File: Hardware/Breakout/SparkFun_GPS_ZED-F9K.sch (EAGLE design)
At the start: 65 parts, among them J1 QWIIC_RIGHT_ANGLE, J4 U.FL, J6 QWIIC_RIGHT_ANGLE, U2 3.3V, U3 UBLOX_ZED_F9R

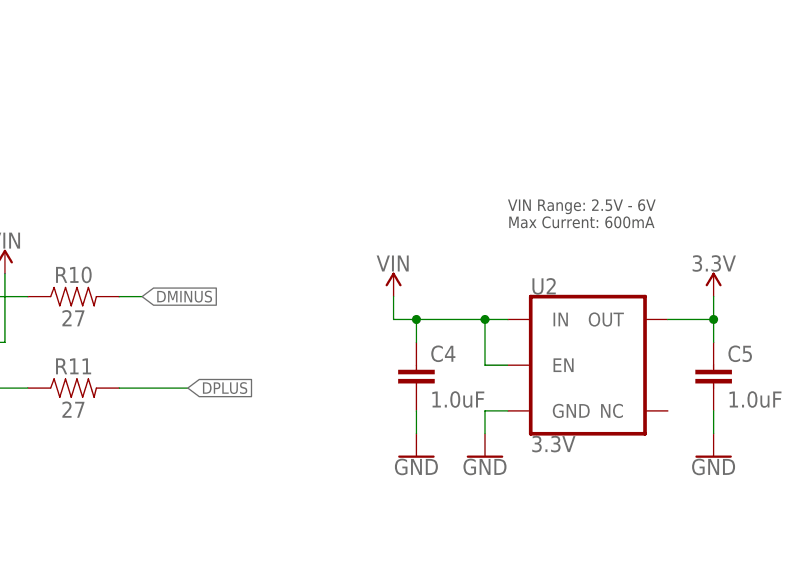
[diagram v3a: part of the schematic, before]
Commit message: Touches up some vias and traces
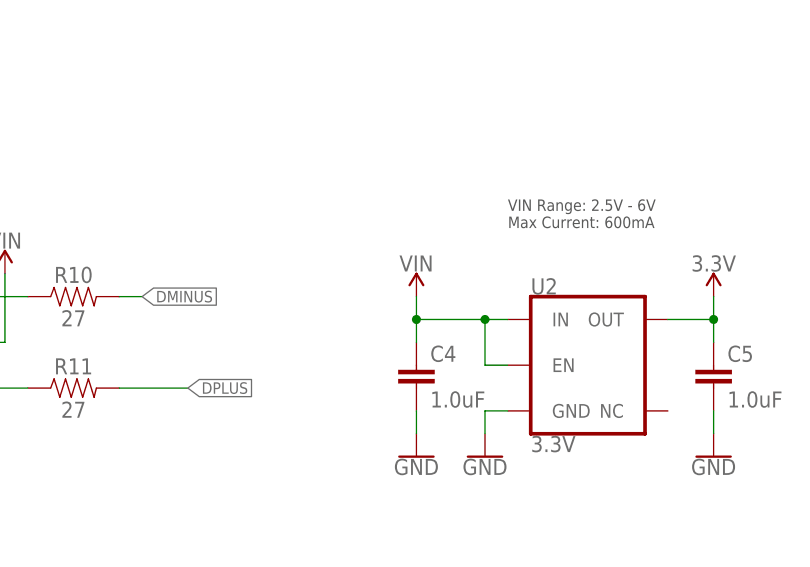
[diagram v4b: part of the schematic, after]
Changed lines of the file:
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@@
 <attribute name="VALUE" x="276.86" y="84.074" size="1.778" layer="96" align="bottom-center"/>
 </instance>
-<instance part="SUPPLY10" gate="G$1" x="276.86" y="228.6" smashed="yes">
-<attribute name="VALUE" x="276.86" y="231.394" size="1.778" layer="96" align="bottom-center"/>
+<instance part="SUPPLY10" gate="G$1" x="279.4" y="228.6" smashed="yes">
+<attribute name="VALUE" x="279.4" y="231.394" size="1.778" layer="96" align="bottom-center"/>
 </instance>
 <instance part="R5" gate="G$1" x="124.46" y="68.58" smashed="yes">
@@
 <wire x1="289.56" y1="226.06" x2="287.02" y2="226.06" width="0.1524" layer="91"/>
 <wire x1="287.02" y1="226.06" x2="279.4" y2="226.06" width="0.1524" layer="91"/>
-<wire x1="279.4" y1="226.06" x2="276.86" y2="226.06" width="0.1524" layer="91"/>
-<wire x1="276.86" y1="226.06" x2="276.86" y2="228.6" width="0.1524" layer="91"/>
+<wire x1="279.4" y1="226.06" x2="279.4" y2="228.6" width="0.1524" layer="91"/>
 <pinref part="U2" gate="G$1" pin="EN"/>
 <wire x1="289.56" y1="220.98" x2="287.02" y2="220.98" width="0.1524" layer="91"/>

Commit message: Gerbers for both boards
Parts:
- removed C5: 1.0uF, SparkFun-Capacitors:1.0UF-0603-16V-10%-X7R
- removed H3: STAND-OFFTIGHT, SparkFun-Hardware:STAND-OFFTIGHT
- removed J8: (no value), SparkFun-Connectors:CONN_09NO_SILK
- removed PPS, PWR: JUMPER-SMT_2_NC_TRACE_SILK, SparkFun-Jumpers:JUMPER-SMT_2_NC_TRACE_SILK
- added $1_36_$_2020-02-13_17-32-45: STAND-OFFTIGHT, SparkFun-Hardware:STAND-OFFTIGHT
- added C3: 1.0uF, SparkFun-Capacitors:1.0UF-0603-16V-10%-X7R
- added J7: (no value), SparkFun-Connectors:CONN_06NO_SILK_NO_POP
- added JP5: JUMPER-SMT_2_NO_SILK, SparkFun-Jumpers:JUMPER-SMT_2_NO_SILK
- added JP6: JUMPER-SMT_3_2-NC_TRACE_SILK, SparkFun-Jumpers:JUMPER-SMT_3_2-NC_TRACE_SILK
- C1: value 47pF -> 1.0uF; device SparkFun-Capacitors:47PF-0603-50V-5% -> SparkFun-Capacitors:1.0UF-0402-16V-10%
- C2: value 1.0uF -> 47pF; device SparkFun-Capacitors:1.0UF-0402-16V-10% -> SparkFun-Capacitors:47PF-0603-50V-5%
- D1: value 0.5A/40V/420mV -> RED; device SparkFun-DiscreteSemi:DIODE-SCHOTTKY-PMEG4005EJ -> SparkFun-LED:LED-RED0603
- D2: value RED -> BLUE; device SparkFun-LED:LED-RED0603 -> SparkFun-LED:LED-BLUE0603
- D4: value PRTR5V0U2F -> BLUE; device SparkFun-IC-Power:PRTR5V0U2F -> SparkFun-LED:LED-BLUE0603
- D5: value BLUE -> PRTR5V0U2F; device SparkFun-LED:LED-BLUE0603 -> SparkFun-IC-Power:PRTR5V0U2F
- D6: value BLUE -> 0.5A/40V/420mV; device SparkFun-LED:LED-BLUE0603 -> SparkFun-DiscreteSemi:DIODE-SCHOTTKY-PMEG4005EJ
- J1: value QWIIC_RIGHT_ANGLE -> U.FL; device SparkFun-Connectors:QWIIC_CONNECTORJS-1MM -> SparkFun-Connectors:U.FL2PIN
- J3: value (none) -> QWIIC_RIGHT_ANGLE; device SparkFun-Connectors:CONN_09NO_SILK -> SparkFun-Connectors:QWIIC_CONNECTORJS-1MM
- J4: value U.FL -> QWIIC_RIGHT_ANGLE; device SparkFun-Connectors:U.FL2PIN -> SparkFun-Connectors:QWIIC_CONNECTORJS-1MM
- J5: device SparkFun-Connectors:CONN_06NO_SILK_NO_POP -> SparkFun-Connectors:CONN_09NO_SILK
- J6: value QWIIC_RIGHT_ANGLE -> (none); device SparkFun-Connectors:QWIIC_CONNECTORJS-1MM -> SparkFun-Connectors:CONN_09NO_SILK
- JP1: value JUMPER-SMT_2_NO_SILK -> JUMPER-SMT_2_NC_TRACE_SILK; device SparkFun-Jumpers:JUMPER-SMT_2_NO_SILK -> SparkFun-Jumpers:JUMPER-SMT_2_NC_TRACE_SILK
- JP2: value JUMPER-SMT_3_2-NC_TRACE_SILK -> JUMPER-SMT_2_NC_TRACE_SILK; device SparkFun-Jumpers:JUMPER-SMT_3_2-NC_TRACE_SILK -> SparkFun-Jumpers:JUMPER-SMT_2_NC_TRACE_SILK
- LOGO1: value SFE_LOGO_NAME_FLAME.2_INCH -> OSHW-LOGOM; device SparkFun-Aesthetics:SFE_LOGO_NAME_FLAME.2_INCH -> SparkFun-Aesthetics:OSHW-LOGOM
- LOGO3: value OSHW-LOGOM -> SFE_LOGO_NAME_FLAME.2_INCH; device SparkFun-Aesthetics:OSHW-LOGOM -> SparkFun-Aesthetics:SFE_LOGO_NAME_FLAME.2_INCH
- R1: value 3.3k -> 100K; device SparkFun-Resistors:3.3KOHM-0603-1/10W-1% -> SparkFun-Resistors:100KOHM-0402-1/16W-1%
- R10, R11: value 27 -> 33; device SparkFun-Resistors:27OHM-0603-1/10W-1% -> SparkFun-Resistors:33OHM-0402-1/10W-1%
- R13, R14, R2: value 1KOHM-0402-1/16W-1% -> 33; device SparkFun-Resistors:1KOHM-0402-1/16W-1% -> SparkFun-Resistors:33OHM-0402-1/10W-1%
- R17: value 33 -> 10; device SparkFun-Resistors:33OHM-0402-1/10W-1% -> SparkFun-Resistors:10OHM-0603-1/10W-1%
- R18, R20: value 33 -> 5.1k; device SparkFun-Resistors:33OHM-0402-1/10W-1% -> SparkFun-Resistors:5.1KOHM-0402-1/16W-1%
- R19, R25: value 33 -> 2.2K; device SparkFun-Resistors:33OHM-0402-1/10W-1% -> SparkFun-Resistors:2.2KOHM-0402-1/16W-1%
- R21, R22, R23, R24: value 33 -> 1KOHM-0402-1/16W-1%; device SparkFun-Resistors:33OHM-0402-1/10W-1% -> SparkFun-Resistors:1KOHM-0402-1/16W-1%
- R26, R27: value 33 -> 27; device SparkFun-Resistors:33OHM-0402-1/10W-1% -> SparkFun-Resistors:27OHM-0603-1/10W-1%
- R28: value 1KOHM-0402-1/16W-1% -> 3.3k; device SparkFun-Resistors:1KOHM-0402-1/16W-1% -> SparkFun-Resistors:3.3KOHM-0603-1/10W-1%
- R3, R4: value 2.2K -> 33; device SparkFun-Resistors:2.2KOHM-0402-1/16W-1% -> SparkFun-Resistors:33OHM-0402-1/10W-1%
- R5: value 10 -> 33; device SparkFun-Resistors:10OHM-0603-1/10W-1% -> SparkFun-Resistors:33OHM-0402-1/10W-1%
- R6: value 100K -> 33; device SparkFun-Resistors:100KOHM-0402-1/16W-1% -> SparkFun-Resistors:33OHM-0402-1/10W-1%
- R8, R9: value 5.1k -> 33; device SparkFun-Resistors:5.1KOHM-0402-1/16W-1% -> SparkFun-Resistors:33OHM-0402-1/10W-1%
- renumbered B1 to BT1, FRAME2 to FRAME1, GEO to JP4, RTK to JP3, U3 to U1
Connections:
- net !RESET: now also J6.4, R4.2; no longer J8.4, R7.2
- net !SAFEBOOT: now also J6.3, R16.2; no longer J8.3, R25.2
- net 3.3V: now also C1.1, C4.1, D6.A, J3.2, J4.2, J5.3, J6.8, JP6.2, R1.2; no longer C2.1, C5.1, D2.A, J1.2, J3.3, J6.2, J8.8, JP2.2, R6.2
- net DIR: now also J5.8, R3.1; no longer J3.8, R27.1
- net DMINUS: now also R26.2; no longer R10.2
- net DPLUS: now also R27.2; no longer R11.2
- net D_SEL: now also JP5.1; no longer JP1.1
- net GEOF_STAT: now also D4.A, R13.2; no longer D3.A, R22.2
- net GND: now also C3.2, D5.2, J1.GND, J4.1, J6.9, J7.1, JP1.1, JP2.1, JP5.2, R1.1, R18.1, R20.1; no longer C5.2, D4.2, J1.1, J4.GND, J6.1, J8.9, JP1.2, PPS.1, PWR.1, R6.1, R8.1, R9.1
- net INT: now also J6.2, R5.2; no longer J8.2, R12.2
- net N$1: now also JP6.1, R25.2; no longer JP2.1, R3.2
- net N$10: now also D5.4, R27.1; no longer D4.4, R11.1
- net N$11: now also R4.1; no longer R7.1
- net N$12: now also R5.1; no longer R12.1
- net N$14: now also R18.2; no longer R8.2
- net N$15: now also R20.2; no longer R9.2
- net N$16: now also R6.1; no longer R15.1
- net N$17: now also R7.1; no longer R16.1
- net N$18: now also R8.1; no longer R17.1
- net N$19: now also R9.1; no longer R18.1
- net N$2: now also D6.C, R28.2; no longer D1.C, R1.2
- net N$20: now also R10.1; no longer R19.1
- net N$21: now also R11.1; no longer R20.1
- net N$22: now also R23.1; no longer R14.1
- net N$23: now also JP2.2, R22.1; no longer PPS.2, R13.1
- net N$24: now also D2.C, R22.2; no longer D5.C, R13.2
- net N$25: now also D3.C, R23.2; no longer D6.C, R14.2
- net N$26: now also R12.1; no longer R21.1
- net N$27: now also R13.1; no longer R22.1
- net N$28: now also R14.1; no longer R23.1
- net N$29: now also R15.1; no longer R24.1
- net N$3: now also JP6.3, R19.2; no longer JP2.3, R4.2
- net N$30: now also R16.1; no longer R25.1
- net N$31: now also R2.2; no longer R26.2
- net N$32: now also R3.2; no longer R27.2
- net N$33: now also R24.1; no longer R28.1
- net N$34: now also D4.C, R24.2; no longer D3.C, R28.2
- net N$4: now also D1.C, R21.2; no longer D2.C, R2.2
- net N$5: now also C2.1, R17.1; no longer C1.1, R5.1
- net N$6: now also D5.3; no longer D4.3
- net N$7: now also D5.1; no longer D4.1
- net N$8: now also JP1.2, R21.1; no longer PWR.2, R2.1
- net N$9: now also D5.6, R26.1; no longer D4.6, R10.1
- net PPS: now also D2.A, J6.1, R15.2; no longer D5.A, J8.1, R24.2
- net RF_IN: now also J1.SIGNAL; no longer J4.SIGNAL
- net RTK_STAT: now also D3.A, R14.2; no longer D6.A, R23.2
- net RXI/MOSI: now also J5.5, R10.2; no longer J3.5, R19.2
- net RXI2: now also J7.4, R12.2; no longer J5.4, R21.2
- net SCL/CLK: now also J3.4, J4.4, J5.7, J6.6, R19.1, R7.2; no longer J1.4, J3.7, J6.4, J8.6, R16.2, R4.1
- net SDA/!CS: now also J3.3, J4.3, J5.4, J6.7, R25.1, R6.2; no longer J1.3, J3.4, J6.3, J8.7, R15.2, R3.1
- net TXO/MISO: now also J5.6, R9.2; no longer J3.6, R18.2
- net TXO2: now also J7.5, R11.2; no longer J5.5, R20.2
- net TX_READY: now also J6.5, R8.2; no longer J8.5, R17.2
- net VIN: now also C3.1, D5.5, J5.2; no longer C4.1, D4.5, J3.2
- net V_BATT: now also R28.1; no longer R1.1
- net V_RF: now also R17.2; no longer R5.2
- net WT: now also J5.9, R2.1; no longer J3.9, R26.1
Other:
- moved on the sheet: C1, C2, C4, D2, D3, R1, R10, R11, R12, R13, R14, R15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

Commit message: Adds automotive certified diode to wt/dir circuitry
* Adds wt/dir circuitry to both breakout board and pi hat
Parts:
- added C12, C15: 1.0nF, SparkFun-Capacitors:1.0NF/1000PF-0402-50V-10%
- added C13, C14: 22nF, SparkFun-Capacitors:22NF/22,000PF-0603-50V-10%
- added C16, C17, C18: 0.1uF, SparkFun-Capacitors:0.1UF-0402-16V-10%
- added D10, D9: 0.5A/40V/420mV, classified:BZX84_DIODE
- added R35, R37: 3.3k, SparkFun-Resistors:3.3KOHM-0603-1/10W-1%
- added R36, R38: 470, SparkFun-Resistors:470OHM-0603-1/10W-1%
- added R39, R40: 910, classified:910OHM-0603-1/10W-5%
- added U$62, U$63: UHS_INVERTER_SCHMITT_TRIGGERSIP6, classified:UHS_INVERTER_SCHMITT_TRIGGERSIP6
- added U4: HCPL-270L, classified:HCPL-270L
- J2: device SparkFun-Connectors:USB_C2-LAYER -> SparkFun-Connectors:USB_C_2-LAYER_PADS
- J5: device SparkFun-Connectors:CONN_09NO_SILK -> SparkFun-Connectors:CONN_111X11_NO_SILK
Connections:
- removed net DIR: J5.8, R3.1
- removed net WT: J5.9, R2.1
- new net DIR+: J5.9, R37.1
- new net DIR-: C12.2, D10.A, J5.8, U4.CATHODE2
- new net DIR_IN: R38.2, U4.ANODE2
- new net DIR_OUT: R3.1, U$63.Y
- new net DIR_SCHMITT: C14.1, R40.1, U$63.A, U4.VOUT2
- new net N$35: C15.1, D9.C, R35.2, R36.1
- new net N$37: C12.1, D10.C, R37.2, R38.1
- new net WT+: J5.11, R35.1
- new net WT-: C15.2, D9.A, J5.10, U4.CATHODE1
- new net WT_IN: R36.2, U4.ANODE1
- new net WT_OUT: R2.1, U$62.Y
- new net WT_SCHMITT: C13.1, R39.1, U$62.A, U4.VOUT1
- net 3.3V: now also C16.1, C17.1, C18.1, R39.2, R40.2, U$62.VCC, U$63.VCC, U4.VCC
- net GND: now also C13.2, C14.2, C16.2, C17.2, C18.2, U$62.GND, U$63.GND, U4.GND
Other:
- note added: "Wheel Tick and Direction Signal"
- note added: "v10"
- note removed: "v01"
- moved on the sheet: C1, C2, C3, C4, D1, D2, D3, D4, D5, FB1, J1, J3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

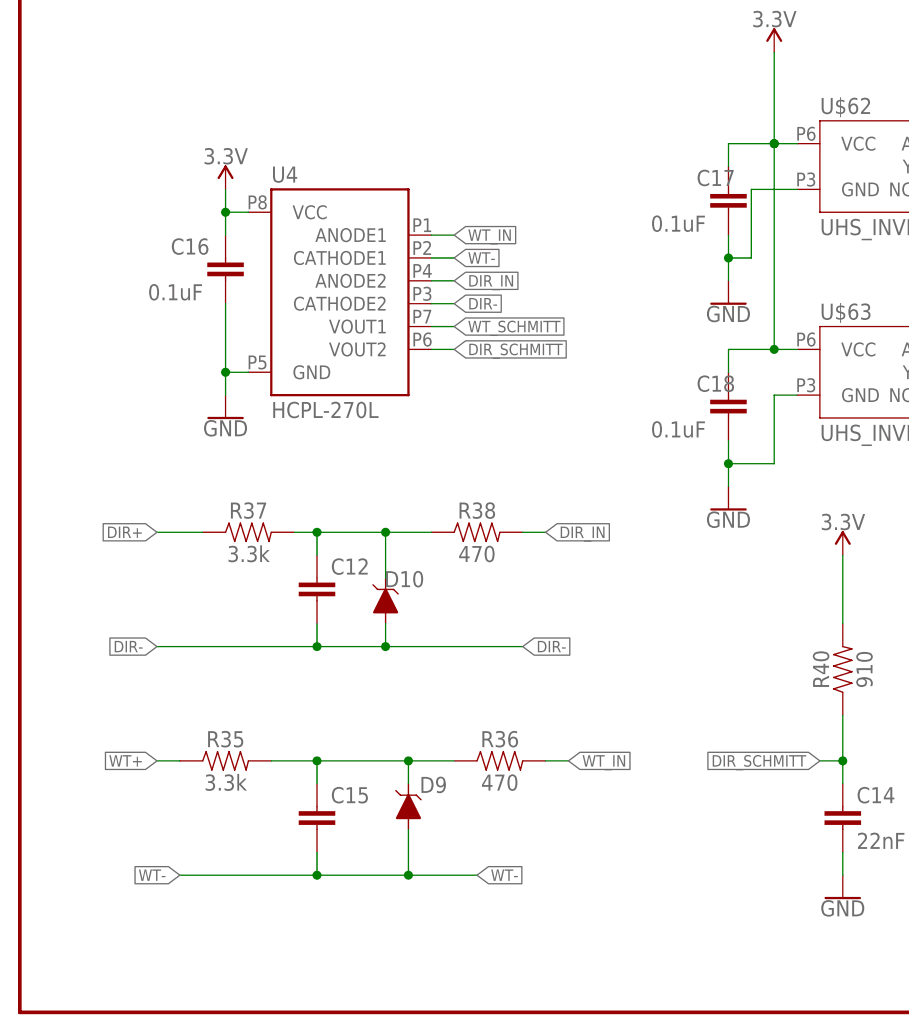
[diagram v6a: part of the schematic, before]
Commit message: Updates designs with new X7R capacitors
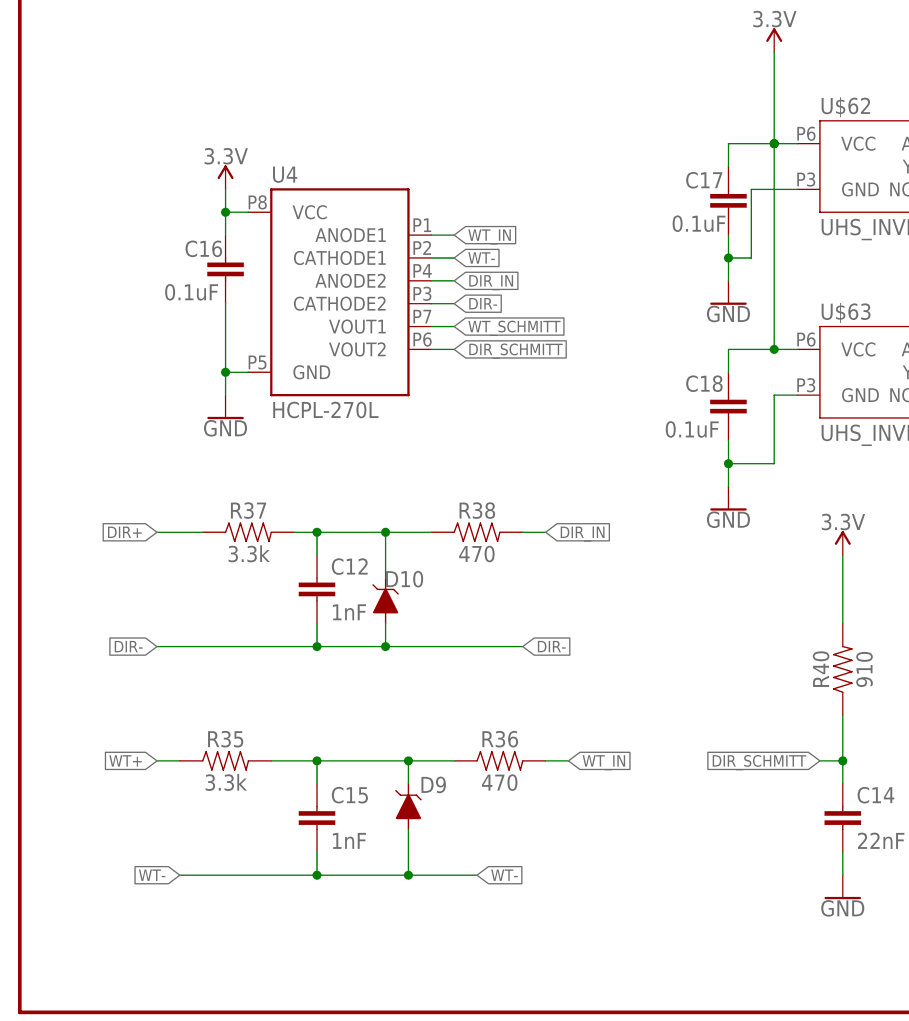
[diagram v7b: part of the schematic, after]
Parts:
- C1: device SparkFun-Capacitors:1.0UF-0402-16V-10% -> SparkFun-Capacitors:1.0UF-0603-16V-10%-X7R
- C12, C15: value 1.0nF -> 1nF; device SparkFun-Capacitors:1.0NF/1000PF-0402-50V-10% -> SparkFun-Capacitors:1.0NF/1000PF-0402-25V-10%-X7R
- C13, C14: device SparkFun-Capacitors:22NF/22,000PF-0603-50V-10% -> SparkFun-Capacitors:22NF/22,000PF-0603-25V-10%-X7R
- C16, C17, C18: device SparkFun-Capacitors:0.1UF-0402-16V-10% -> SparkFun-Capacitors:0.1UF-0402-6.3V-10%-X7R
- C2: device SparkFun-Capacitors:47PF-0603-50V-5% -> SparkFun-Capacitors:47PF-0402-25V-5%-X7R
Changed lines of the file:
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@@
 <part name="J2" library="SparkFun-Connectors" deviceset="USB_C" device="_2-LAYER_PADS"/>
 <part name="FRAME1" library="SparkFun-Aesthetics" deviceset="FRAME-LEDGER" device=""/>
-<part name="C2" library="SparkFun-Capacitors" deviceset="47PF" device="-0603-50V-5%" value="47pF"/>
+<part name="C2" library="SparkFun-Capacitors" deviceset="47PF" device="-0402-25V-5%-X7R" value="47pF"/>
 <part name="U2" library="SparkFun-IC-Power" deviceset="V_REG_AP2112" device="K-3.3V" value="3.3V"/>
 <part name="R18" library="SparkFun-Resistors" deviceset="5.1KOHM" device="-0402-1/16W-1%" value="5.1k"/>
@@
 <part name="SUPPLY1" library="SparkFun-PowerSymbols" deviceset="V_BATT" device=""/>
 <part name="U1" library="classified" deviceset="UBLOX_ZED_F9R" device=""/>
-<part name="C1" library="SparkFun-Capacitors" deviceset="1.0UF" device="-0402-16V-10%" value="1.0uF"/>
+<part name="C1" library="SparkFun-Capacitors" deviceset="1.0UF" device="-0603-16V-10%-X7R" value="1.0uF"/>
 <part name="SUPPLY3" library="SparkFun-PowerSymbols" deviceset="3.3V" device=""/>
 <part name="R1" library="SparkFun-Resistors" deviceset="100KOHM" device="-0402-1/16W-1%" value="100K"/>
@@
 <part name="R37" library="SparkFun-Resistors" deviceset="3.3KOHM" device="-0603-1/10W-1%" value="3.3k"/>
 <part name="R38" library="SparkFun-Resistors" deviceset="470OHM" device="-0603-1/10W-1%" value="470"/>
-<part name="C12" library="SparkFun-Capacitors" deviceset="1.0NF/1000PF" device="-0402-50V-10%" value="1.0nF"/>
-<part name="C13" library="SparkFun-Capacitors" deviceset="22NF/22,000PF" device="-0603-50V-10%" value="22nF"/>
-<part name="C14" library="SparkFun-Capacitors" deviceset="22NF/22,000PF" device="-0603-50V-10%" value="22nF"/>
-<part name="C15" library="SparkFun-Capacitors" deviceset="1.0NF/1000PF" device="-0402-50V-10%" value="1.0nF"/>
+<part name="C12" library="SparkFun-Capacitors" deviceset="1.0NF/1000PF" device="-0402-25V-10%-X7R" value="1nF"/>
+<part name="C13" library="SparkFun-Capacitors" deviceset="22NF/22,000PF" device="-0603-25V-10%-X7R" value="22nF"/>
+<part name="C14" library="SparkFun-Capacitors" deviceset="22NF/22,000PF" device="-0603-25V-10%-X7R" value="22nF"/>
+<part name="C15" library="SparkFun-Capacitors" deviceset="1.0NF/1000PF" device="-0402-25V-10%-X7R" value="1nF"/>
 <part name="D9" library="classified" deviceset="BZX84_DIODE" device="" value="0.5A/40V/420mV"/>
 <part name="R39" library="classified" deviceset="910OHM-0603-1/10W-5%" device="" value="910"/>
 <part name="R40" library="classified" deviceset="910OHM-0603-1/10W-5%" device="" value="910"/>
 <part name="U4" library="classified" deviceset="HCPL-270L" device=""/>
-<part name="C16" library="SparkFun-Capacitors" deviceset="0.1UF" device="-0402-16V-10%" value="0.1uF"/>
+<part name="C16" library="SparkFun-Capacitors" deviceset="0.1UF" device="-0402-6.3V-10%-X7R" value="0.1uF"/>
 <part name="SUPPLY21" library="SparkFun-PowerSymbols" deviceset="3.3V" device=""/>
 <part name="GND25" library="SparkFun-PowerSymbols" deviceset="GND" device=""/>
@@
 <part name="SUPPLY23" library="SparkFun-PowerSymbols" deviceset="3.3V" device=""/>
 <part name="SUPPLY24" library="SparkFun-PowerSymbols" deviceset="3.3V" device=""/>
-<part name="C17" library="SparkFun-Capacitors" deviceset="0.1UF" device="-0402-16V-10%" value="0.1uF"/>
-<part name="C18" library="SparkFun-Capacitors" deviceset="0.1UF" device="-0402-16V-10%" value="0.1uF"/>
+<part name="C17" library="SparkFun-Capacitors" deviceset="0.1UF" device="-0402-6.3V-10%-X7R" value="0.1uF"/>
+<part name="C18" library="SparkFun-Capacitors" deviceset="0.1UF" device="-0402-6.3V-10%-X7R" value="0.1uF"/>
 <part name="GND29" library="SparkFun-PowerSymbols" deviceset="GND" device=""/>
 </parts>
@@
 <instance part="C12" gate="G$1" x="33.02" y="45.72" smashed="yes">
 <attribute name="NAME" x="34.544" y="48.641" size="1.778" layer="95" font="vector"/>
+<attribute name="VALUE" x="34.544" y="43.561" size="1.778" layer="96" font="vector"/>
 </instance>
 <instance part="C13" gate="G$1" x="124.46" y="20.32" smashed="yes">
@@
 <instance part="C15" gate="G$1" x="33.02" y="20.32" smashed="yes">
 <attribute name="NAME" x="34.544" y="23.241" size="1.778" layer="95" font="vector"/>
+<attribute name="VALUE" x="34.544" y="18.161" size="1.778" layer="96" font="vector"/>
 </instance>
 <instance part="D9" gate="G$1" x="43.18" y="22.86" smashed="yes" rot="R90">
@@
 </instance>
 <instance part="C16" gate="G$1" x="22.86" y="81.28" smashed="yes">
-<attribute name="NAME" x="16.764" y="84.201" size="1.778" layer="95" font="vector"/>
-<attribute name="VALUE" x="14.224" y="79.121" size="1.778" layer="96" font="vector"/>
+<attribute name="NAME" x="18.288" y="83.947" size="1.778" layer="95" font="vector"/>
+<attribute name="VALUE" x="16.002" y="79.121" size="1.778" layer="96" font="vector"/>
 </instance>
 <instance part="SUPPLY21" gate="G$1" x="22.86" y="91.44" smashed="yes">
@@
 </instance>
 <instance part="C17" gate="G$1" x="78.74" y="88.9" smashed="yes">
-<attribute name="NAME" x="75.184" y="91.821" size="1.778" layer="95" font="vector"/>
-<attribute name="VALUE" x="70.104" y="86.741" size="1.778" layer="96" font="vector"/>
+<attribute name="NAME" x="73.914" y="91.567" size="1.778" layer="95" font="vector"/>
+<attribute name="VALUE" x="72.39" y="86.741" size="1.778" layer="96" font="vector"/>
 </instance>
 <instance part="C18" gate="G$1" x="78.74" y="66.04" smashed="yes">
-<attribute name="NAME" x="75.184" y="68.961" size="1.778" layer="95" font="vector"/>
-<attribute name="VALUE" x="70.104" y="63.881" size="1.778" layer="96" font="vector"/>
+<attribute name="NAME" x="73.914" y="68.961" size="1.778" layer="95" font="vector"/>
+<attribute name="VALUE" x="71.628" y="63.881" size="1.778" layer="96" font="vector"/>
 </instance>
 <instance part="GND29" gate="1" x="78.74" y="78.74" smashed="yes">
